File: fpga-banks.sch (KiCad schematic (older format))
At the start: 21 parts, among them U1 XC7K70T-FBG484, U2 ASEM1-100.000MHZ-LC-T

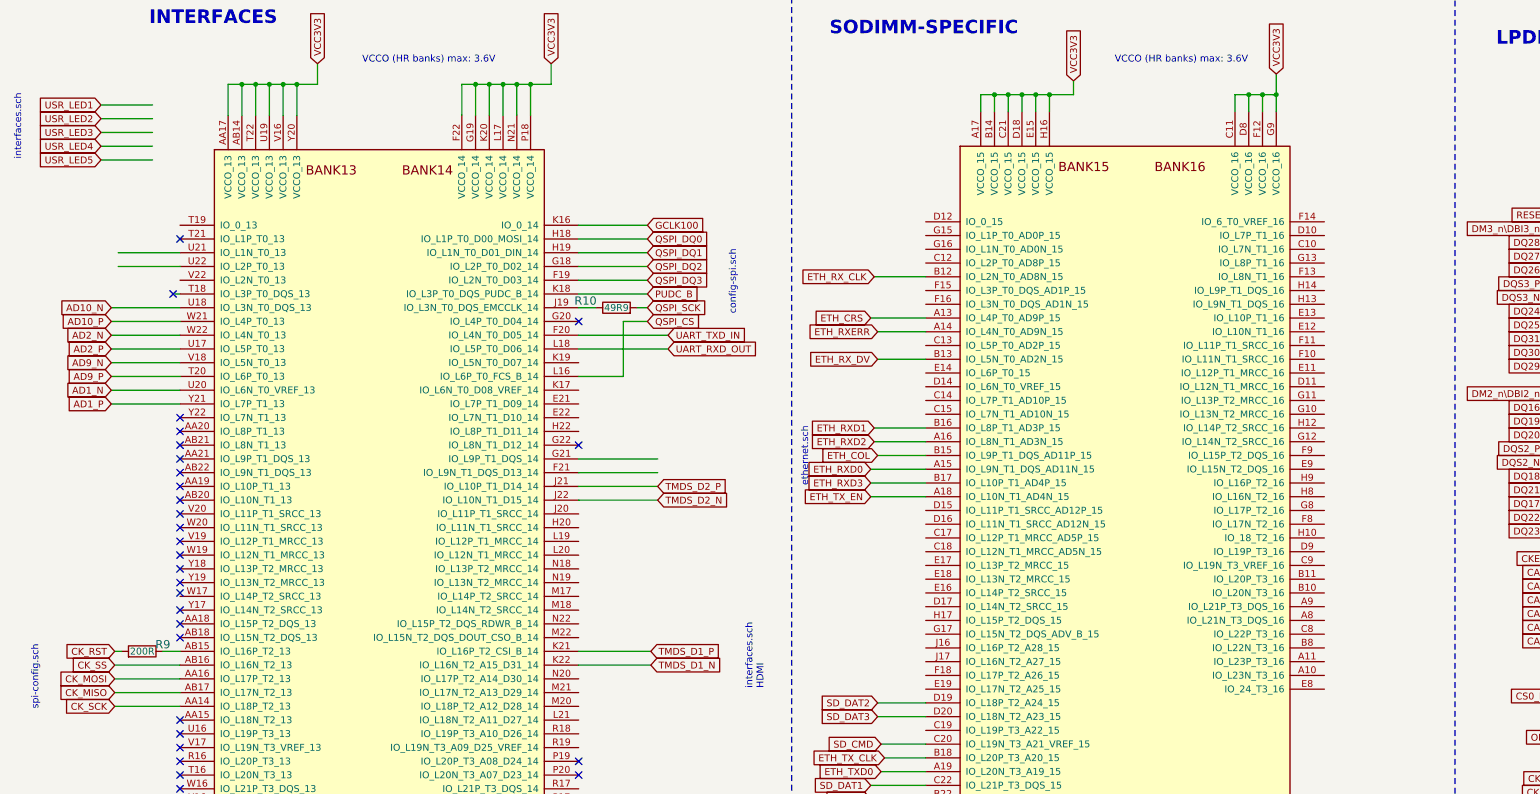
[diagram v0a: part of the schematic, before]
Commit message: Route USR LEDs
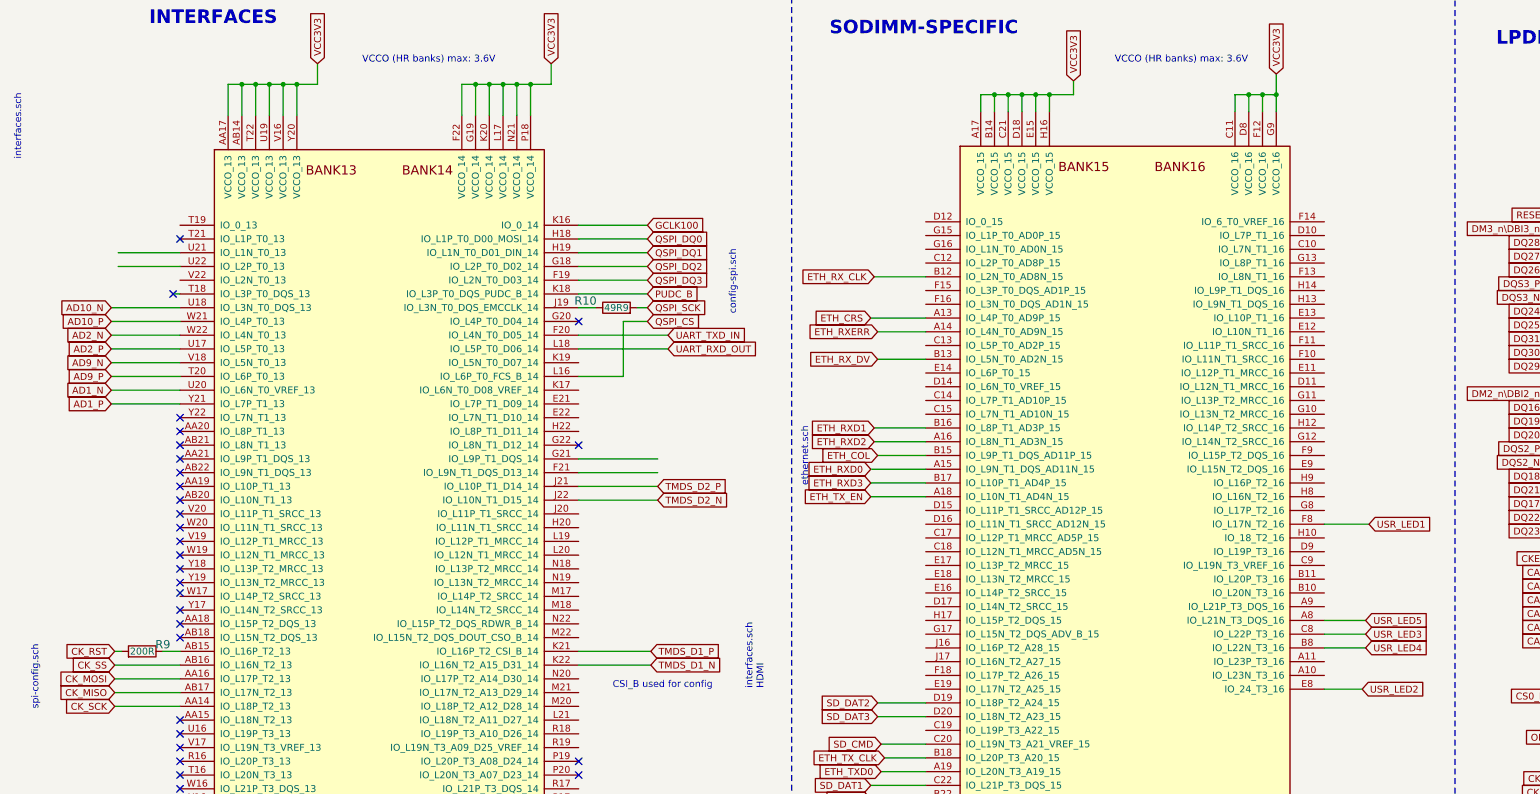
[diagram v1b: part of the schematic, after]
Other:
- note added: "CSI_B used for config"
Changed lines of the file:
@@
 Text Notes 5950 2950 1    50   ~ 0
 config-spi.sch
-Wire Wire Line
-	1700 1425 1325 1425
-Text GLabel 1325 1425 0    50   Input ~ 0
+Text GLabel 10550 4475 2    50   Input ~ 0
 USR_LED1
-Wire Wire Line
-	1700 1525 1325 1525
-Text GLabel 1325 1525 0    50   Input ~ 0
+Text GLabel 10500 5675 2    50   Input ~ 0
 USR_LED2
-Wire Wire Line
-	1700 1625 1325 1625
-Text GLabel 1325 1625 0    50   Input ~ 0
+Text GLabel 10525 5275 2    50   Input ~ 0
 USR_LED3
-Wire Wire Line
-	1700 1725 1325 1725
-Text GLabel 1325 1725 0    50   Input ~ 0
+Text GLabel 10525 5375 2    50   Input ~ 0
 USR_LED4
-Wire Wire Line
-	1700 1825 1325 1825
-Text GLabel 1325 1825 0    50   Input ~ 0
+Text GLabel 10525 5175 2    50   Input ~ 0
 USR_LED5
 Wire Wire Line
@@
 Wire Wire Line
 	6975 5775 7325 5775
+Text Notes 5775 5675 2    50   ~ 0
+CSI_B used for config
+Wire Wire Line
+	10550 4475 10225 4475
+Wire Wire Line
+	10225 5675 10500 5675
+Wire Wire Line
+	10225 5175 10525 5175
+Wire Wire Line
+	10225 5275 10525 5275
+Wire Wire Line
+	10225 5375 10525 5375
 $EndSCHEMATC

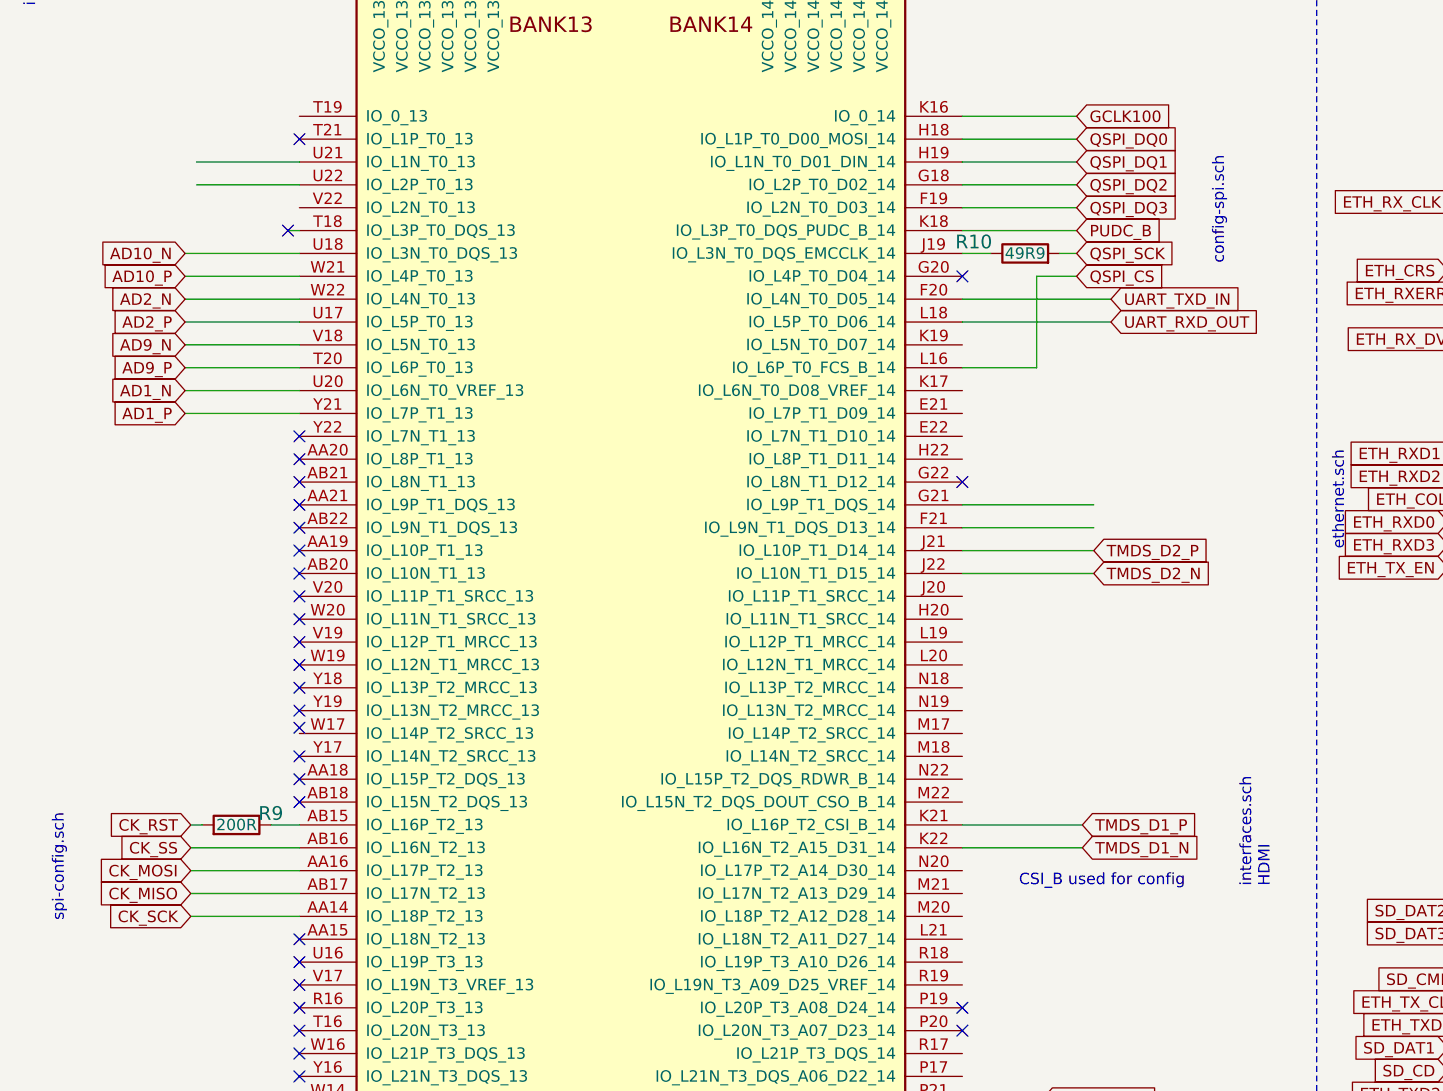
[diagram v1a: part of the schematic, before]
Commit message: Update SPI configuration setup
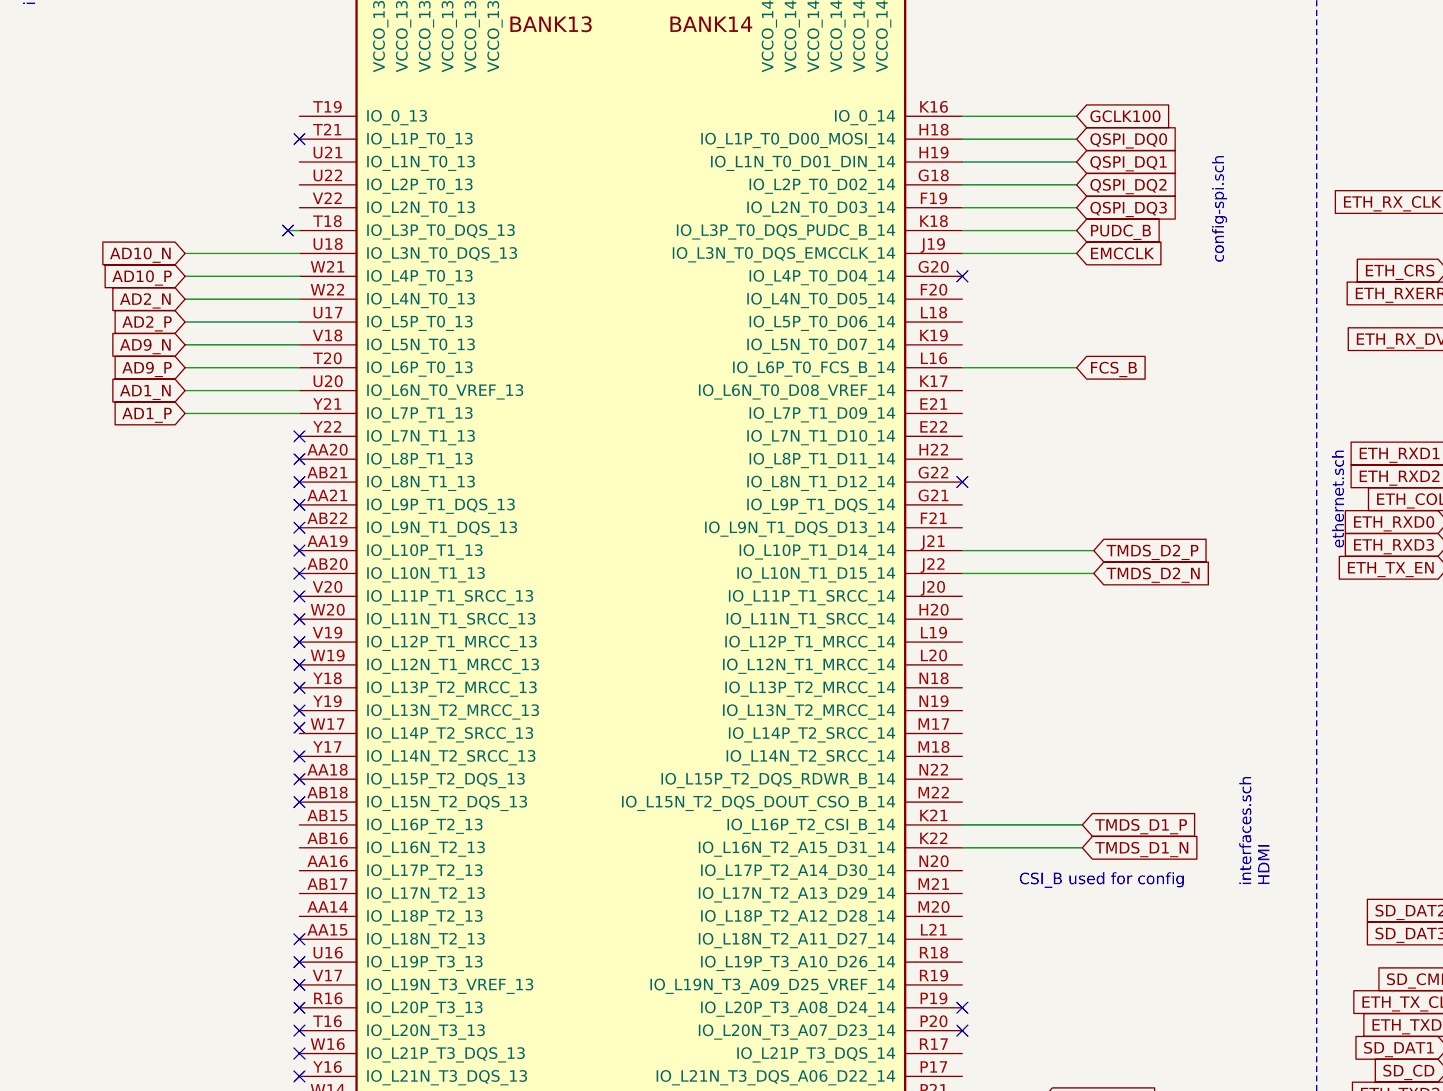
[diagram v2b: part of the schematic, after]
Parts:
- removed R10: R_49R9_0402, lpddr4-test-board-footprints:0402-res, symbol lpddr4-test-board:R_49R9_0402
- removed R9: R_200R_0402, lpddr4-test-board-footprints:0402-res, symbol lpddr4-test-board:R_200R_0402
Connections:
- net labels added: EMCCLK, FCS_B
- net labels removed: CK_MISO, CK_MOSI, CK_SCK, CK_SS, QSPI_CS, QSPI_SCK, UART_RXD_OUT, UART_TXD_IN
- wire segments 297 -> 282
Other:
- note removed: "spi-config.sch"
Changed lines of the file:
@@
 Text GLabel 1400 2900 0    50   Input ~ 0
 AD10_N
-Wire Wire Line
-	4800 3200 5450 3200
-Wire Wire Line
-	4800 3100 5450 3100
-Text GLabel 5450 3100 2    50   Input ~ 0
-UART_TXD_IN
-Text GLabel 5450 3200 2    50   Input ~ 0
-UART_RXD_OUT
 Text GLabel 8150 8700 0    50   Input ~ 0
 VSNS5V0_P
@@
 $EndComp
 Wire Wire Line
-	4800 4100 5375 4100
-Wire Wire Line
-	4800 4000 5375 4000
-Wire Wire Line
 	4800 2300 5300 2300
 Text Notes 6475 4200 1    50   ~ 0
@@
 	12025 4625 12025 5825
 Text GLabel 5300 2900 2    50   Input ~ 0
-QSPI_SCK
+EMCCLK
 Text GLabel 5300 2400 2    50   Input ~ 0
 QSPI_DQ0
@@
 Text GLabel 5300 2600 2    50   Input ~ 0
 QSPI_DQ2
-Text GLabel 5300 3000 2    50   Input ~ 0
-QSPI_CS
+Text GLabel 5300 3400 2    50   Input ~ 0
+FCS_B
 Text GLabel 5300 2500 2    50   Input ~ 0
 QSPI_DQ1
@@
 Wire Wire Line
 	4800 2800 5300 2800
-$Comp
-L lpddr4-test-board:R_49R9_0402 R?
-U 1 1 69FB6CA6
-P 5075 2900
-AR Path="/5FD53C7D/69FB6CA6" Ref="R?"  Part="1"
-AR Path="/5F96C515/69FB6CA6" Ref="R10"  Part="1"
-F 0 "R10" H 4850 2950 60  0000 C CNN
-F 1 "R_49R9_0402" H 5075 2750 60  0001 C CNN
-F 2 "lpddr4-test-board-footprints:0402-res" H 5275 3100 60  0001 L CNN
-F 3 "" H 5075 2900 50  0001 C CNN
-F 4 "VISHAY" H 5275 3300 60  0001 L CNN "Manufacturer"
-F 5 "CRCW040249R9FKED" H 5275 3200 60  0001 L CNN "MPN"
-F 6 "49R9" H 5075 2900 50  0000 C CNN "Val"
-	1    5075 2900
-	1    0    0    -1
-$EndComp
-Wire Wire Line
-	4800 2900 4925 2900
-Wire Wire Line
-	5225 2900 5300 2900
-Wire Wire Line
-	5125 3400 5125 3000
-Wire Wire Line
-	5125 3000 5300 3000
-Wire Wire Line
-	5125 3400 4800 3400
 Text Notes 5950 2950 1    50   ~ 0
 config-spi.sch
@@
 Text GLabel 13150 1050 1    50   Input ~ 0
 VDDQ
-Wire Wire Line
-	1900 5400 1775 5400
-Wire Wire Line
-	1425 5400 1475 5400
-$Comp
-L lpddr4-test-board:R_200R_0402 R9
-U 1 1 6B4FB04F
-P 1625 5400
-F 0 "R9" H 1475 5450 60  0000 C CNN
-F 1 "R_200R_0402" H 1625 5250 60  0001 C CNN
-F 2 "lpddr4-test-board-footprints:0402-res" H 1825 5600 60  0001 L CNN
-F 3 "" H 1625 5400 50  0001 C CNN
-F 4 "YAGEO" H 1825 5800 60  0001 L CNN "Manufacturer"
-F 5 "RC0402FR-07200RL" H 1825 5700 60  0001 L CNN "MPN"
-F 6 "200R" H 1625 5400 50  0000 C CNN "Val"
-	1    1625 5400
-	-1   0    0    -1
-$EndComp
-Wire Wire Line
-	1900 5800 1425 5800
-Wire Wire Line
-	1900 5700 1425 5700
-Wire Wire Line
-	1900 5600 1425 5600
-Wire Wire Line
-	1900 5500 1425 5500
-Text GLabel 1425 5500 0    50   Input ~ 0
-CK_SS
-Text GLabel 1425 5800 0    50   Input ~ 0
-CK_SCK
-Text GLabel 1425 5700 0    50   Input ~ 0
-CK_MISO
-Text GLabel 1425 5600 0    50   Input ~ 0
-CK_MOSI
-Text GLabel 1425 5400 0    50   Input ~ 0
-CK_RST
-Text Notes 875  5825 1    50   ~ 0
-spi-config.sch
 Text Notes 750  1825 1    50   ~ 0
 interfaces.sch
@@
 NoConn ~ 1900 6800
 NoConn ~ 1900 6900
-NoConn ~ 1900 7000
-NoConn ~ 1900 7100
-NoConn ~ 1900 7200
 NoConn ~ 4800 3000
 NoConn ~ 4800 3900
@@
 Wire Wire Line
 	4800 7100 5150 7100
-Wire Wire Line
-	1450 2500 1900 2500
-Wire Wire Line
-	1450 2600 1900 2600
 NoConn ~ 1900 2400
 Wire Wire Line
@@
 Wire Wire Line
 	10225 5375 10525 5375
+Wire Wire Line
+	4800 3400 5300 3400
+Wire Wire Line
+	4800 2900 5300 2900
+NoConn ~ 1900 7000
+NoConn ~ 1900 7100
+NoConn ~ 1900 7200
 $EndSCHEMATC

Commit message: Routed configuration block
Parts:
- removed C3: C_820p_0603, lpddr4-test-board-footprints:0603-res, symbol lpddr4-test-board:C_820p_0603
- removed R15, R17: R_200R_0402, lpddr4-test-board-footprints:0402-res, symbol lpddr4-test-board:R_200R_0402
- removed R16: R_10k_0402, lpddr4-test-board-footprints:0402-res, symbol lpddr4-test-board:R_10k_0402
- removed S1: B3U-1000P, lpddr4-test-board-footprints:Switch_Tactile_SMD_B3U-1000P, symbol lpddr4-test-board:B3U-1000P
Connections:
- net labels removed: CK_RST
- wire segments 282 -> 272
- no-connect marks 58 -> 59
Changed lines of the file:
@@
 Text GLabel 10200 8700 2    50   Input ~ 0
 AD1_P
-Wire Wire Line
-	5050 10375 5600 10375
-Wire Wire Line
-	5050 8825 5550 8825
-Wire Wire Line
-	5050 9325 5500 9325
-Text GLabel 5975 9325 2    50   Input ~ 0
-CK_RST
-$Comp
-L lpddr4-test-board:R_10k_0402 R16
-U 1 1 5FBBB45F
-P 5050 9075
-F 0 "R16" V 4900 9100 60  0000 L CNN
-F 1 "R_10k_0402" H 5050 8925 60  0001 C CNN
-F 2 "lpddr4-test-board-footprints:0402-res" H 5250 9275 60  0001 L CNN
-F 3 "" H 5050 9075 50  0001 C CNN
-F 4 "VISHAY" H 5250 9475 60  0001 L CNN "Manufacturer"
-F 5 "CRCW040210K0FKEDHP" H 5250 9375 60  0001 L CNN "MPN"
-F 6 "10k" V 5200 9100 50  0000 L CNN "Val"
-	1    5050 9075
-	0    1    1    0
-$EndComp
-Wire Wire Line
-	5050 8825 5050 8925
-Wire Wire Line
-	5050 9325 5050 9225
 $Comp
 L lpddr4-test-board:R_100R_0402 R1
@@
 Wire Wire Line
 	9650 9000 10200 9000
-$Comp
-L lpddr4-test-board:GND #PWR0103
-U 1 1 60A83D37
-P 5600 10425
-F 0 "#PWR0103" H 5600 10175 50  0001 C CNN
-F 1 "GND" H 5605 10252 50  0000 C CNN
-F 2 "" H 5600 10425 50  0001 C CNN
-F 3 "" H 5600 10425 50  0001 C CNN
-	1    5600 10425
-	1    0    0    -1
-$EndComp
-Wire Wire Line
-	5600 10375 5600 10425
-Text GLabel 5550 8825 1    50   Input ~ 10
-VCC3V3
-$Comp
-L lpddr4-test-board:R_200R_0402 R17
-U 1 1 60B10DCB
-P 5050 9550
-F 0 "R17" V 4900 9575 60  0000 L CNN
-F 1 "R_200R_0402" H 5050 9400 60  0001 C CNN
-F 2 "lpddr4-test-board-footprints:0402-res" H 5250 9750 60  0001 L CNN
-F 3 "" H 5050 9550 50  0001 C CNN
-F 4 "YAGEO" H 5250 9950 60  0001 L CNN "Manufacturer"
-F 5 "RC0402FR-07200RL" H 5250 9850 60  0001 L CNN "MPN"
-F 6 "200R" V 5200 9600 50  0000 L CNN "Val"
-	1    5050 9550
-	0    1    1    0
-$EndComp
-Wire Wire Line
-	5050 9400 5050 9325
-Connection ~ 5050 9325
-$Comp
-L lpddr4-test-board:B3U-1000P S1
-U 1 1 60B66561
-P 5050 10025
-F 0 "S1" V 4997 10163 60  0000 L CNN
-F 1 "B3U-1000P" V 5103 10163 60  0000 L CNN
-F 2 "lpddr4-test-board-footprints:Switch_Tactile_SMD_B3U-1000P" H 5250 10225 60  0001 L CNN
-F 3 "https://omronfs.omron.com/en_US/ecb/products/pdf/en-b3u.pdf" H 5250 10325 60  0001 L CNN
-F 4 "B3U-1000P" H 5250 10525 60  0001 L CNN "MPN"
-F 5 "Omron Electronics Inc-EMC Div" H 5250 11125 60  0001 L CNN "Manufacturer"
-	1    5050 10025
-	0    1    1    0
-$EndComp
-Wire Wire Line
-	5050 10225 5050 10375
-Wire Wire Line
-	5050 9825 5050 9700
 Text GLabel 5150 7000 2    50   Input ~ 0
 TMDS_CLK_P
@@
 Text GLabel 6975 5775 0    50   Input ~ 0
 SD_DAT2
-$Comp
-L lpddr4-test-board:R_200R_0402 R15
-U 1 1 60AC14D7
-P 5650 9325
-F 0 "R15" H 5425 9375 60  0000 C CNN
-F 1 "R_200R_0402" H 5650 9175 60  0001 C CNN
-F 2 "lpddr4-test-board-footprints:0402-res" H 5850 9525 60  0001 L CNN
-F 3 "" H 5650 9325 50  0001 C CNN
-F 4 "YAGEO" H 5850 9725 60  0001 L CNN "Manufacturer"
-F 5 "RC0402FR-07200RL" H 5850 9625 60  0001 L CNN "MPN"
-F 6 "200R" H 5650 9325 50  0000 C CNN "Val"
-	1    5650 9325
-	1    0    0    -1
-$EndComp
-Wire Wire Line
-	4800 2300 5300 2300
 Text Notes 6475 4200 1    50   ~ 0
 ethernet.sch
@@
 Text GLabel 7000 6075 0    50   Input ~ 0
 SD_CMD
-Text GLabel 5300 2300 2    50   Input ~ 0
-GCLK100
 Text GLabel 6975 5875 0    50   Input ~ 0
 SD_DAT3
@@
 Text Notes 1675 850  0    98   ~ 20
 INTERFACES
-Wire Wire Line
-	5800 9325 5975 9325
 Wire Wire Line
 	14125 9000 14325 9000
@@
 Text Notes 8700 1125 0    50   ~ 0
 VCCO (HR banks) max: 3.6V
-$Comp
-L lpddr4-test-board:C_820p_0603 C3
-U 1 1 604141EE
-P 9675 9900
-F 0 "C3" H 9790 9945 60  0000 L CNN
-F 1 "C_820p_0603" H 9675 9750 60  0001 C CNN
-F 2 "lpddr4-test-board-footprints:0603-res" H 9875 10100 60  0001 L CNN
-F 3 "" H 9675 9900 50  0001 C CNN
-F 4 "KEMET" H 9875 10300 60  0001 L CNN "Manufacturer"
-F 5 "C0603C821J5RACTU" H 9875 10200 60  0001 L CNN "MPN"
-F 6 "820p" H 9790 9847 50  0000 L CNN "Val"
-	1    9675 9900
-	1    0    0    -1
-$EndComp
 NoConn ~ 1850 2800
 NoConn ~ 1900 3700
@@
 NoConn ~ 1900 7100
 NoConn ~ 1900 7200
+Text GLabel 5300 3600 2    50   Input ~ 0
+GCLK100
+Wire Wire Line
+	4800 3600 5300 3600
+NoConn ~ 4800 2300
 $EndSCHEMATC

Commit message: Cleanup
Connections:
- net GND: no longer U1.AA1 (IO_L22P_T3_34), U1.K4 (IO_0_VRN_34), U1.L4 (IO_L6N_T0_VREF_34), U1.P5 (IO_L18N_T2_34), U1.T3 (IO_L12N_T1_MRCC_34)
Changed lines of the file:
@@
-$EndComp
-Wire Wire Line
-	15000 2225 15075 2225
-Wire Wire Line
-	15075 2225 15075 3425
-Wire Wire Line
-	15000 6525 15075 6525
-Connection ~ 15075 6525
-Wire Wire Line
-	15075 6525 15075 7475
-Wire Wire Line
-	15000 5825 15075 5825
-Connection ~ 15075 5825
-Wire Wire Line
-	15075 5825 15075 6525
-Wire Wire Line
-	15000 4625 15075 4625
-Connection ~ 15075 4625
-Wire Wire Line
-	15075 4625 15075 5825
-Wire Wire Line
-	15000 3425 15075 3425
-Connection ~ 15075 3425
-Wire Wire Line
-	15075 3425 15075 4625
-$Comp
-L lpddr4-test-board:GND #PWR0105
-U 1 1 686D88A2
-P 15075 7475
-F 0 "#PWR0105" H 15075 7225 50  0001 C CNN
-F 1 "GND" H 15080 7302 50  0000 C CNN
-F 2 "" H 15075 7475 50  0001 C CNN
-F 3 "" H 15075 7475 50  0001 C CNN
-	1    15075 7475
-	1    0    0    -1
 $EndComp
 Wire Wire Line
